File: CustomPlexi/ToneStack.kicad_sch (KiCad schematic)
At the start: 12 parts, among them SW4 Pedal Enable, SW5 Plexi Channel Select

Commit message: commit
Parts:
- C6: footprint Capacitor_SMD_AKL:C_0603_1608Metric -> Capacitor_SMD:C_0402_1005Metric_Pad0.74x0.62mm_HandSolder
- R6: footprint Resistor_SMD_AKL:R_0603_1608Metric -> Resistor_SMD:R_0402_1005Metric_Pad0.72x0.64mm_HandSolder
- RV3, RV4: footprint (none) -> PCM_Potentiometer_THT_US_AKL_Double:Potentiometer_Vishay_148-149_Single_Vertical
- SW4: footprint (none) -> CustomLib:SW_SPST_x3_PinHeader2.54mm
- SW5: footprint (none) -> CustomLib:SW_SPST_x4_PinHeader2.54mm
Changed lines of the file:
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@@
       (effects (font (size 1.27 1.27)))
     )
-    (property "Footprint" "Resistor_SMD_AKL:R_0603_1608Metric" (at 106.68 78.74 0)
+    (property "Footprint" "Resistor_SMD:R_0402_1005Metric_Pad0.72x0.64mm_HandSolder" (at 106.68 78.74 0)
       (effects (font (size 1.27 1.27)) hide)
     )
@@
       (effects (font (size 1.27 1.27)) (justify right))
     )
-    (property "Footprint" "" (at 130.81 101.6 0)
+    (property "Footprint" "PCM_Potentiometer_THT_US_AKL_Double:Potentiometer_Vishay_148-149_Single_Vertical" (at 130.81 101.6 0)
       (effects (font (size 1.27 1.27)) hide)
     )
@@
       (effects (font (size 1.27 1.27)))
     )
-    (property "Footprint" "" (at 227.33 95.25 0)
+    (property "Footprint" "CustomLib:SW_SPST_x3_PinHeader2.54mm" (at 227.33 95.25 0)
       (effects (font (size 1.27 1.27)) hide)
     )
@@
       (effects (font (size 1.27 1.27)) (justify right))
     )
-    (property "Footprint" "" (at 158.75 95.25 0)
+    (property "Footprint" "PCM_Potentiometer_THT_US_AKL_Double:Potentiometer_Vishay_148-149_Single_Vertical" (at 158.75 95.25 0)
       (effects (font (size 1.27 1.27)) hide)
     )
@@
       (effects (font (size 1.27 1.27)))
     )
-    (property "Footprint" "" (at 151.13 81.28 0)
+    (property "Footprint" "CustomLib:SW_SPST_x4_PinHeader2.54mm" (at 151.13 81.28 0)
       (effects (font (size 1.27 1.27)) hide)
     )
@@
       (effects (font (size 1.27 1.27)))
     )
-    (property "Footprint" "Capacitor_SMD_AKL:C_0603_1608Metric" (at 119.38 113.3348 0)
+    (property "Footprint" "Capacitor_SMD:C_0402_1005Metric_Pad0.74x0.62mm_HandSolder" (at 119.38 113.3348 0)
       (effects (font (size 1.27 1.27)) hide)
     )
@@
       (effects (font (size 1.27 1.27)))
     )
-    (property "Footprint" "" (at 203.2 92.71 0)
+    (property "Footprint" "CustomLib:SW_SPST_x4_PinHeader2.54mm" (at 203.2 92.71 0)
       (effects (font (size 1.27 1.27)) hide)
     )
@@
       (effects (font (size 1.27 1.27)) (justify right))
     )
-    (property "Footprint" "" (at 130.81 114.3 0)
+    (property "Footprint" "PCM_Potentiometer_THT_US_AKL_Double:Potentiometer_Vishay_148-149_Single_Vertical" (at 130.81 114.3 0)
       (effects (font (size 1.27 1.27)) hide)
     )
@@
       (effects (font (size 1.27 1.27)) (justify right))
     )
-    (property "Footprint" "" (at 130.81 86.36 0)
+    (property "Footprint" "PCM_Potentiometer_THT_US_AKL_Double:Potentiometer_Vishay_148-149_Single_Vertical" (at 130.81 86.36 0)
       (effects (font (size 1.27 1.27)) hide)
     )
@@
       (effects (font (size 1.27 1.27)) (justify right))
     )
-    (property "Footprint" "" (at 170.18 95.25 0)
+    (property "Footprint" "PCM_Potentiometer_THT_US_AKL_Double:Potentiometer_Vishay_148-149_Single_Vertical" (at 170.18 95.25 0)
       (effects (font (size 1.27 1.27)) hide)
     )
@@
       (effects (font (size 1.27 1.27)))
     )
-    (property "Footprint" "Capacitor_SMD_AKL:C_0603_1608Metric" (at 121.92 93.0148 0)
+    (property "Footprint" "Capacitor_SMD:C_0402_1005Metric_Pad0.74x0.62mm_HandSolder" (at 121.92 93.0148 0)
       (effects (font (size 1.27 1.27)) hide)
     )
@@
       (effects (font (size 1.27 1.27)))
     )
-    (property "Footprint" "Capacitor_SMD_AKL:C_0603_1608Metric" (at 121.92 77.7748 0)
+    (property "Footprint" "Capacitor_SMD:C_0402_1005Metric_Pad0.74x0.62mm_HandSolder" (at 121.92 77.7748 0)
       (effects (font (size 1.27 1.27)) hide)
     )
@@
       (effects (font (size 1.27 1.27)) (justify right))
     )
-    (property "Footprint" "Resistor_SMD_AKL:R_0603_1608Metric" (at 105.41 74.93 0)
-      (effects (font (size 1.27 1.27)) hide)
-    )
+    (property "Footprint" "Resistor_SMD:R_0402_1005Metric_Pad0.72x0.64mm_HandSolder" (at 105.41 74.93 0)
+      (effects (font (size 1.27 1.27)) hide)
+    )

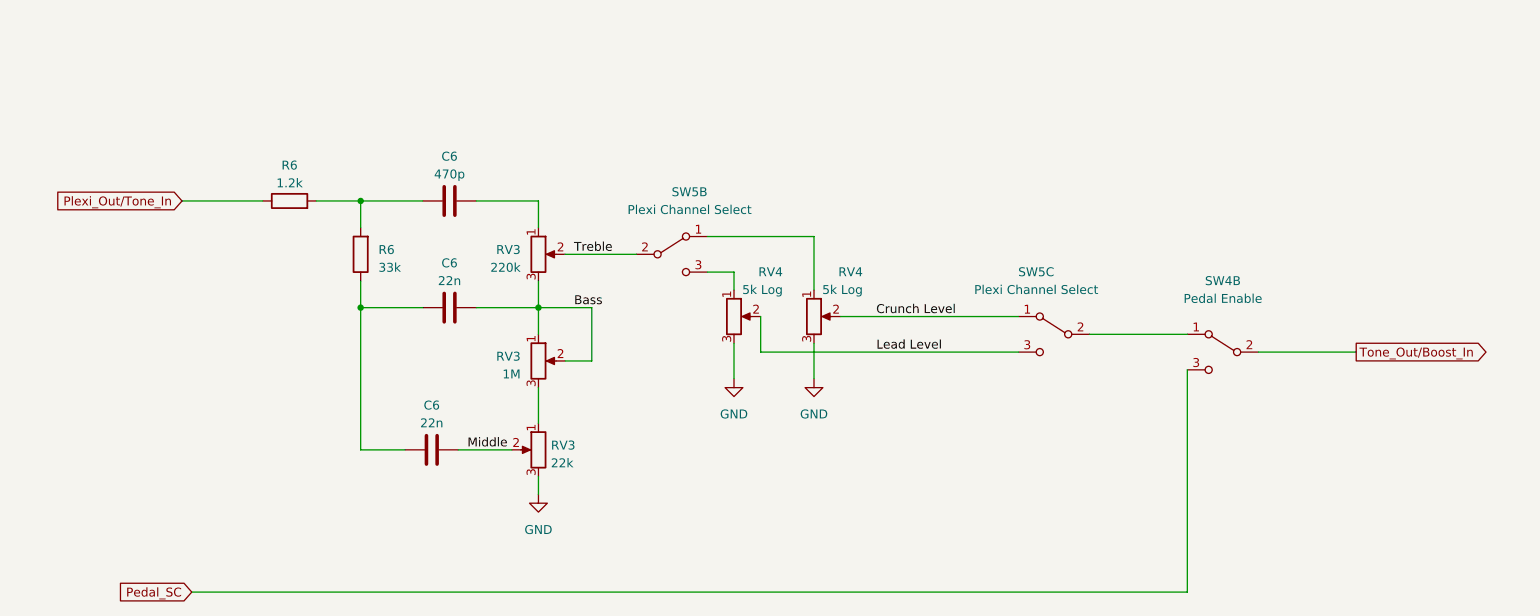
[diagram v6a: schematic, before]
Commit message: deleted tone stack
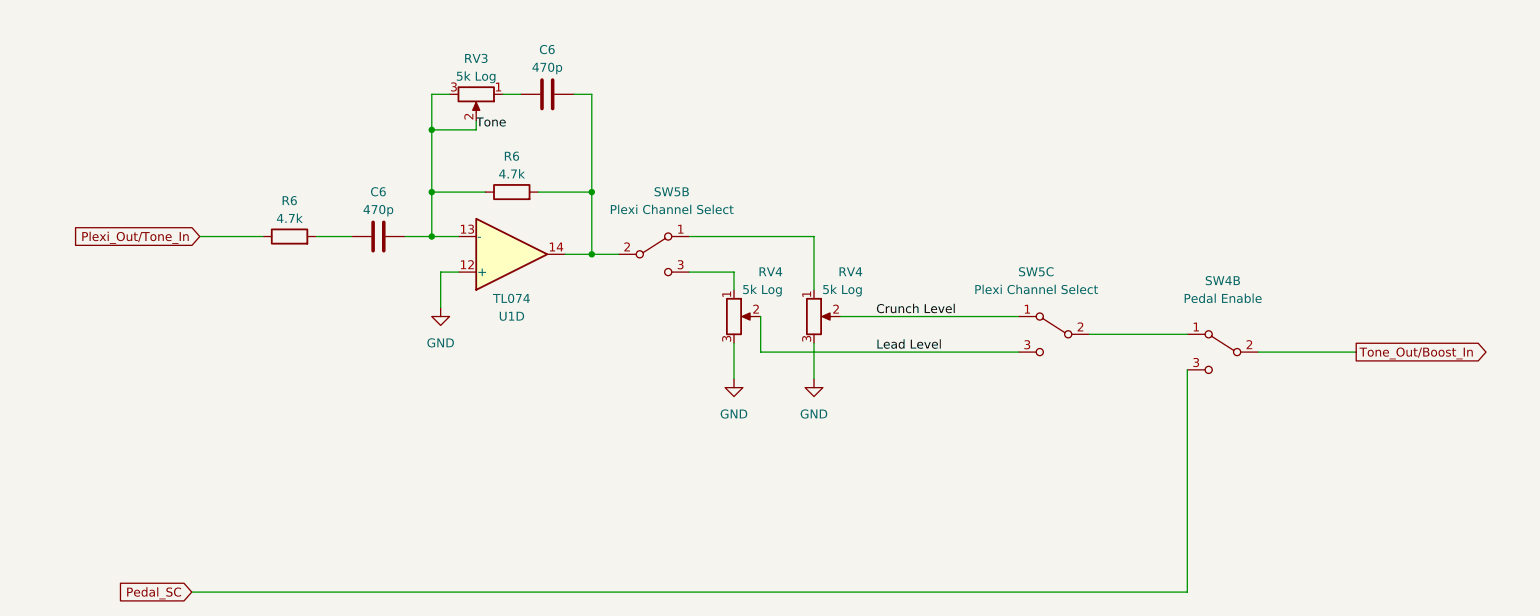
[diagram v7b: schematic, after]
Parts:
- removed C6 (x2): 22n, Capacitor_SMD:C_0402_1005Metric_Pad0.74x0.62mm_HandSolder, symbol PCM_Capacitor_AKL:C_0603
- removed RV3: 1M, PCM_Potentiometer_THT_US_AKL_Double:Potentiometer_Vishay_148-149_Single_Vertical, symbol Device:R_Potentiometer
- removed RV3: 22k, PCM_Potentiometer_THT_US_AKL_Double:Potentiometer_Vishay_148-149_Single_Vertical, symbol Device:R_Potentiometer
- removed RV3: 220k, PCM_Potentiometer_THT_US_AKL_Double:Potentiometer_Vishay_148-149_Single_Vertical, symbol Device:R_Potentiometer
- added C6: 470p, Capacitor_SMD:C_0402_1005Metric_Pad0.74x0.62mm_HandSolder, symbol PCM_Capacitor_AKL:C_0603
- added RV3: 5k Log, PCM_Potentiometer_THT_US_AKL_Double:Potentiometer_Vishay_148-149_Single_Vertical, symbol Device:R_Potentiometer
- added U1: TL074, Package_SO:SOIC-14W_7.5x9mm_P1.27mm, symbol Amplifier_Operational:TL074
- R6: value 1.2k -> 4.7k
- R6: value 33k -> 4.7k
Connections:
- net GND: now also U1.12 (+)
- net at C6.1, R6.2: no longer R6.2
- net Tone: now reaches R6.1
- net Tone: now also C6.2, RV3.2, RV3.3, U1.13 (-)
- net Treble: no longer names the net of SW5.2
- net Treble: now also R6.2, C6.2, U1.14
- new net: C6.1, RV3.1
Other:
- moved on the sheet: C6, R6, SW5B
